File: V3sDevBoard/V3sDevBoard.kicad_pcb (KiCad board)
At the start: 2 copper layers, 100 x 80 mm, 197 parts, among them J1 JST_ETHERNET, J10 Power, J2 USB_C_Receptacle_USB2.0_16P, J3 USB_C_Receptacle_USB2.0_16P, J4 Micro_SD_Card_Det1, J5 LCD, J6 MIPI CSI, J7 JST_I2C, J8 AudioJack, J9 GPIO, SW1 BUT6, SW2 BUT1, SW3 BUT2, SW4 BUT3, SW5 BUT4, SW6 BUT5, U1 Allwinner_V3s, U10 MPU-6050, U11 BME280, U12 USBLC6-2SC6, U13 USBLC6-2SC6, U14 USBLC6-2SC6, U15 USBLC6-2SC6, U16 USBLC6-2SC6, U2 SY8089AAAC, U3 SY8089AAAC, U4 SY8089AAAC, U5 CH340C, U6 PT4103, U8 ESP32-WROOM-32, U9 Ai-Thinker-Ra-02, Y1 32768, Y2 24M

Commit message: first attempts to arrange components on a PCB
plus making footprints bme280&mpu6050 easier to hand solder.
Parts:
- BT1, C17: moved to B.Cu
- C43, C44: footprint Capacitor_SMD:C_0201_0603Metric_Pad0.64x0.40mm_HandSolder -> Capacitor_SMD:C_0603_1608Metric_Pad1.08x0.95mm_HandSolder
- L1, L2, L3, L4: footprint Inductor_SMD:L_APV_APH0420 -> Inductor_SMD:L_APV_APH0420_HandSolder
- Y1: value 32768 -> 24M; footprint Crystal:Crystal_SMD_Abracon_ABS25-4Pin_8.0x3.8mm -> Crystal:Crystal_SMD_3225-4Pin_3.2x2.5mm_HandSoldering
- Y2: footprint Crystal:Crystal_HC49-4H_Vertical -> Crystal:Crystal_SMD_3225-4Pin_3.2x2.5mm_HandSoldering
- moved D5 252.6 mm to (268.0, 109.5)
- moved D6 252.6 mm to (268.0, 116.1)
- moved D7 252.6 mm to (268.0, 122.7)
- moved D8 252.6 mm to (268.0, 129.4)
- moved SW1 242.4 mm to (219.4, 145.0), turned to -90 degrees
- moved TP14 215.9 mm to (260.2, 119.7)
- moved TP16 215.9 mm to (260.2, 122.7)
- moved TP17 215.9 mm to (260.2, 125.8)
- moved TP13 215.9 mm to (260.2, 116.6)
- moved TP9 215.9 mm to (260.2, 113.5)
- moved R36 215.3 mm to (237.2, 128.8)
- moved SW6 214.6 mm to (211.0, 145.0), turned to -90 degrees
- moved SW5 210.7 mm to (202.5, 145.0), turned to -90 degrees
- moved SW4 207.1 mm to (193.8, 145.0), turned to -90 degrees
- moved SW3 204.2 mm to (185.0, 145.0), turned to -90 degrees
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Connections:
- net LCD_LED_A renamed LED_A
- net LCD_LED_K renamed LED_K
- Y1 pad 1: Net-(U1B-X32KOUT) -> unconnected-(Y1-Pad1)
- Y1 pad 2: (no net) -> Net-(U1B-X32KIN)
- Y1 pad 3: (no net) -> unconnected-(Y1-Pad3)
- Y1 pad 4: Net-(U1B-X32KIN) -> Net-(U1B-X32KOUT)
- Y2 pad 1: Net-(U1B-X24MOUT) -> unconnected-(Y2-Pad1)
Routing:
- net GND: track 0.00 -> 69.4 mm, vias 0 -> 4
- net +3.3V: track 0.00 -> 52.7 mm, vias 0 -> 1
- net +1.8V: track 0.00 -> 31.3 mm
- net +1.2V: track 0.00 -> 31.3 mm
- net Net-(JP7-A): track 0.00 -> 28.6 mm
- net Net-(JP5-A): track 0.00 -> 27.8 mm
- net Net-(JP4-A): track 0.00 -> 27.8 mm
- net Net-(JP3-B): track 0.00 -> 13.8 mm
- net Net-(J7-Pin_1): track 0.00 -> 11.5 mm
- net Net-(U3-FB): track 0.00 -> 10.0 mm
- net Net-(U4-FB): track 0.00 -> 10.0 mm
- net Net-(U2-FB): track 0.00 -> 9.06 mm
- net Net-(U11-CSB): track 0.00 -> 7.82 mm
- net Net-(JP2-A): track 0.00 -> 6.34 mm
- net RA_RESET: track 0.00 -> 5.47 mm
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
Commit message: completing pcb desgin
Returning to project after month away. Switching to 4-layer desgin on 3313 stackup sig-gnd-pow-sig, changing size of some passive to 0603, connecting all components, adding silkscreen.
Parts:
- removed C10: 860u, Capacitor_THT:CP_Radial_D6.3mm_P2.50mm
- removed F1: PCB fuse, Fuse:Fuse_1206_3216Metric
- removed J10: Power, Connector_PinHeader_2.54mm:PinHeader_1x02_P2.54mm_Vertical
- removed R24, R25, R26, R27: 150R, Resistor_SMD:R_0805_2012Metric_Pad1.20x1.40mm_HandSolder
- removed TP18: CAM_IO0, TestPoint:TestPoint_Pad_D1.0mm
- removed TP3: ESPTX, TestPoint:TestPoint_Pad_D1.0mm
- removed TP4: EXPRX, TestPoint:TestPoint_Pad_D1.0mm
- added C22: 100n, Capacitor_SMD:C_0805_2012Metric_Pad1.18x1.45mm_HandSolder, F.Cu at (235.3, 123.8)
- added G***: LOGO, Lib:linux, F.Cu at (233.8, 134.2)
- BT1: footprint Battery:BatteryHolder_MYOUNG_BS-07-A1BJ001_CR2032 -> Connector_PinHeader_1.00mm:PinHeader_1x02_P1.00mm_Vertical_SMD_Pin1Right
- C27, C28, C30, C31, C33, C34, C35, C41, C42: footprint Capacitor_SMD:C_0805_2012Metric_Pad1.18x1.45mm_HandSolder -> Capacitor_SMD:C_0603_1608Metric_Pad1.08x0.95mm_HandSolder
- C32, C36, C37, C38, C39, D5, D6, D7, D8, J4, TP13, TP14, TP16, TP17, TP9: moved to B.Cu
- J9: value GPIO -> Conn_01x07_Pin; footprint Connector_PinHeader_2.54mm:PinHeader_1x10_P2.54mm_Vertical -> Connector_PinHeader_2.54mm:PinHeader_1x07_P2.54mm_Vertical
- R1, R10, R11, R12, R13, R2, R20, R21, R23, R28, R29, R3, R30, R31, R32, R33, R34, R35, R36, R37, R38, R39, R4, R40, R41, R42, R44, R45, R48, R49, R5, R50, R51, R52, R53, R54, R55, R56, R58, R6, R60, R61, R62, R68, R69, R70, R71, R72, R8, R9: footprint Resistor_SMD:R_0805_2012Metric_Pad1.20x1.40mm_HandSolder -> Resistor_SMD:R_0603_1608Metric_Pad0.98x0.95mm_HandSolder
- R14, R15, R16, R17, R18: footprint Resistor_SMD:R_0805_2012Metric_Pad1.20x1.40mm_HandSolder -> Resistor_SMD:R_0603_1608Metric_Pad0.98x0.95mm_HandSolder; moved to B.Cu
- R46, R47: footprint Resistor_SMD:R_1206_3216Metric -> Resistor_SMD:R_0805_2012Metric
- SW1, SW2, SW3, SW4, SW5, SW6: footprint Button_Switch_THT:SW_PUSH_6mm -> Button_Switch_SMD:Button_6x3mm
- U12, U13, U14, U15, U16: value USBLC6-2SC6 -> USBLC6
- Y1: value 24M -> 32K
- moved R35 209.6 mm to (240.0, 75.2)
- moved R28 207.5 mm to (230.3, 104.0), turned to -90 degrees
- moved R71 204.6 mm to (241.0, 101.3), turned to 90 degrees
- moved R72 202.1 mm to (239.0, 101.3), turned to -90 degrees
- moved R62 200.9 mm to (235.4, 104.0), turned to -90 degrees
- moved R61 199.7 mm to (232.8, 104.0), turned to -90 degrees
- moved R32 190.4 mm to (218.6, 86.9), turned to -90 degrees
- moved R30 188.6 mm to (213.8, 86.9), turned to -90 degrees
- moved R33 188.4 mm to (217.0, 86.9), turned to -90 degrees
- moved R31 186.8 mm to (212.2, 86.9), turned to -90 degrees
- moved R34 186.4 mm to (215.4, 86.9), turned to -90 degrees
- moved J9 184.7 mm to (227.8, 108.4), turned to 90 degrees
- moved C29 172.8 mm to (242.3, 77.5)
- moved JP1 170.2 mm to (238.0, 77.5)
- moved R68 164.7 mm to (186.0, 136.0), turned to 90 degrees
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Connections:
- C11 pad 1: EPHY-RX- -> Net-(C11-Pad1)
- C12 pad 1: EPHY-RX+ -> Net-(C12-Pad1)
- C13 pad 1: EPHY-TX- -> Net-(C13-Pad1)
- C14 pad 1: EPHY-TX+ -> Net-(C14-Pad1)
- D5 pad 1: VCC -> +3.3V
- D6 pad 1: VCC -> +3.3V
- D7 pad 1: VCC -> +3.3V
- D8 pad 1: VCC -> +3.3V
- J7 pad 2: TWI0_SDA -> Net-(J7-Pin_2)
- J7 pad 3: TWI0_SCK -> Net-(J7-Pin_3)
- J9 pad 1: Net-(J9-Pin_1) -> GND
- J9 pad 5: Net-(J9-Pin_5) -> VCC
- J9 pad 6: Net-(J9-Pin_6) -> +3.3V
- J9 pad 7: Net-(J9-Pin_7) -> GND
- R28 pad 2: Net-(J9-Pin_5) -> Net-(J9-Pin_2)
- R44 pad 2: VCC -> Net-(U12-VBUS)
- R45 pad 1: VCC -> Net-(U12-VBUS)
- R61 pad 2: Net-(J9-Pin_6) -> Net-(J9-Pin_3)
- R62 pad 2: Net-(J9-Pin_7) -> Net-(J9-Pin_4)
- U14 pad 4: EPHY-RX+ -> Net-(C12-Pad1)
- U14 pad 6: EPHY-RX- -> Net-(C11-Pad1)
- U15 pad 4: EPHY-TX+ -> Net-(C14-Pad1)
- U15 pad 6: EPHY-TX- -> Net-(C13-Pad1)
- U16 pad 4: TWI0_SCK -> Net-(J7-Pin_3)
- U16 pad 5: Net-(J7-Pin_1) -> +3.3V
- U16 pad 6: TWI0_SDA -> Net-(J7-Pin_2)
- Y1 pad 1: unconnected-(Y1-Pad1) -> GND
- Y1 pad 3: unconnected-(Y1-Pad3) -> GND
- Y2 pad 1: unconnected-(Y2-Pad1) -> GND
- Y2 pad 3: unconnected-(Y2-Pad3) -> GND
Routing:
- net VCC: track 0.00 -> 157.6 mm, vias 0 -> 2
- net GND: track 69.4 -> 222.3 mm, vias 4 -> 126
- net TWI0_SDA: track 3.34 -> 142.3 mm, vias 0 -> 6
- net TWI0_SCK: track 3.30 -> 131.3 mm, vias 0 -> 4
- net LED_A: track 0.00 -> 99.6 mm, vias 0 -> 1
- net +3.3V: track 52.7 -> 150.5 mm, vias 1 -> 40
- net +1.2V: track 31.3 -> 127.1 mm, vias 0 -> 14
- net LED_K: track 0.00 -> 89.9 mm, vias 0 -> 1
- net HPCOM: track 0.00 -> 77.3 mm, vias 0 -> 2
- net LCD_LED_PWM: track 0.00 -> 75.3 mm, vias 0 -> 2
- net +1.8V: track 31.3 -> 105.8 mm, vias 0 -> 9
- net UART0_TX: track 0.00 -> 73.8 mm, vias 0 -> 2
- net CSI_SCK: track 0.00 -> 73.5 mm, vias 0 -> 3
- net Net-(D6-DOUT): track 0.00 -> 73.0 mm
- net CSI_SDA: track 0.00 -> 72.7 mm, vias 0 -> 3
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- added copper zone on In2.Cu, net +3.3V
- added copper zone on In1.Cu, net GND
- added copper zone on In2.Cu, net GND
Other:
- board size 100 x 80 mm -> 100 x 85 mm
- copper layers 2 -> 4
- board text added: "GND 3V3 VCC SDA SCK PF6 GND"
- board text added: "GND PF6 SCK SDA VCC 3V3 GND"
- board text added: "J.K 2026.02 V3sDevBoard rev.A"
- board text added: "V3sDevBoard"
- board text added: "github.com/sentoxo/V3sDevBoard"

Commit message: last changes and sending to manufacturing
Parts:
- added R24: 1K, Resistor_SMD:R_0603_1608Metric_Pad0.98x0.95mm_HandSolder, F.Cu at (220.1, 86.9)
- moved D1 1.66 mm to (215.3, 80.9)
- moved C24 1.33 mm to (216.2, 96.1)
- moved C25 1.33 mm to (216.2, 98.3)
- moved R29 1.33 mm to (216.1, 94.3)
- moved R64 0.53 mm to (184.4, 96.4)
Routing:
- net +3.3V: track 150.5 -> 148.0 mm
- net LCD_VSYNC: track 11.1 -> 9.79 mm
- net +3V: track 42.3 -> 41.0 mm
- net GND: track 222.3 -> 221.1 mm, vias 126 -> 128
- net ESP32_UART_RX: track 55.4 -> 54.4 mm
- net Net-(U1A-VRA2): track 14.9 -> 14.1 mm
- net SDC1_D2: track 35.7 -> 36.5 mm
- net Net-(U1A-VRA1): track 12.3 -> 11.6 mm
- net LCD_HSYNC: track 13.8 -> 13.1 mm
- net ESP32_UART_TX: track 58.4 -> 57.7 mm
- net LCD_CLK: track 8.12 -> 7.42 mm
- net LCD_B7: track 18.9 -> 19.5 mm

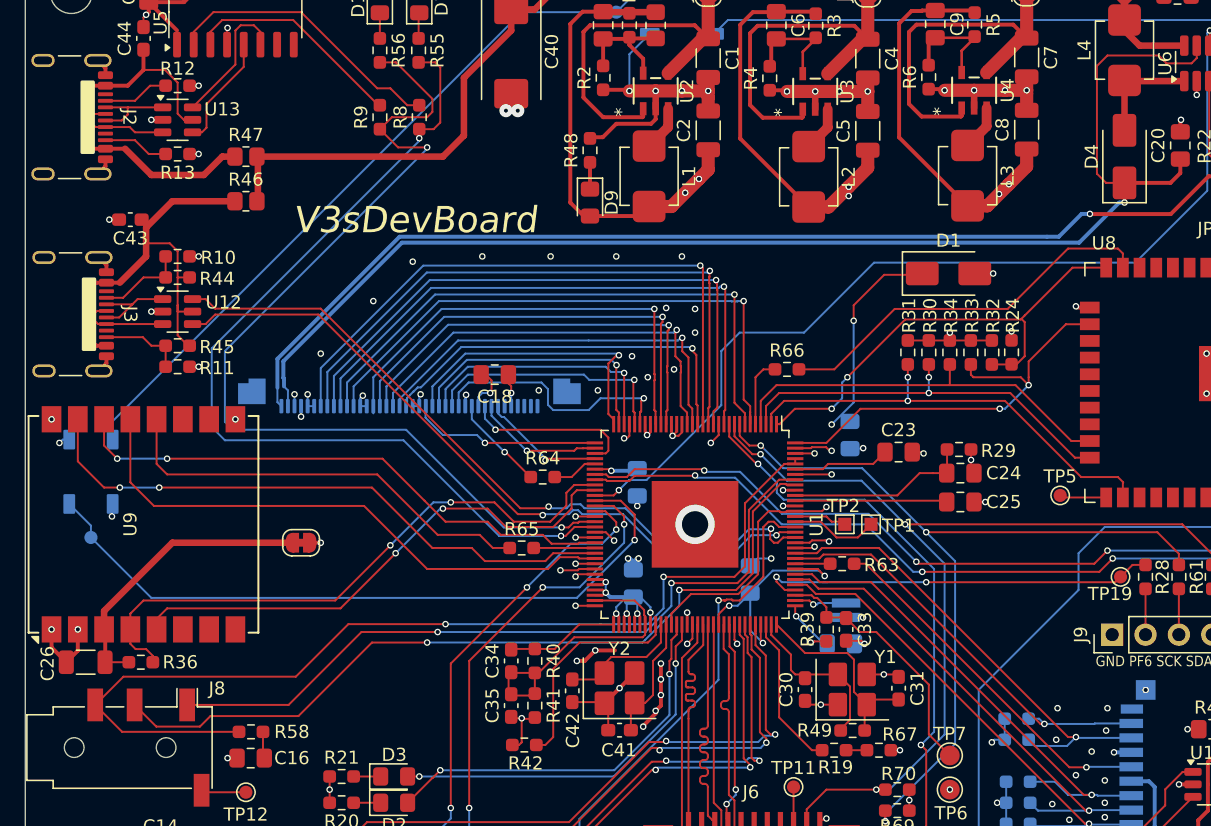
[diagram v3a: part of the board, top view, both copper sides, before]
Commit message: fixing errors in revA
Fixing:
- Ther was mistake in SDIO for SDCard. Swaped data lines.
- RTC didn't have power without battery.
Updating readme.
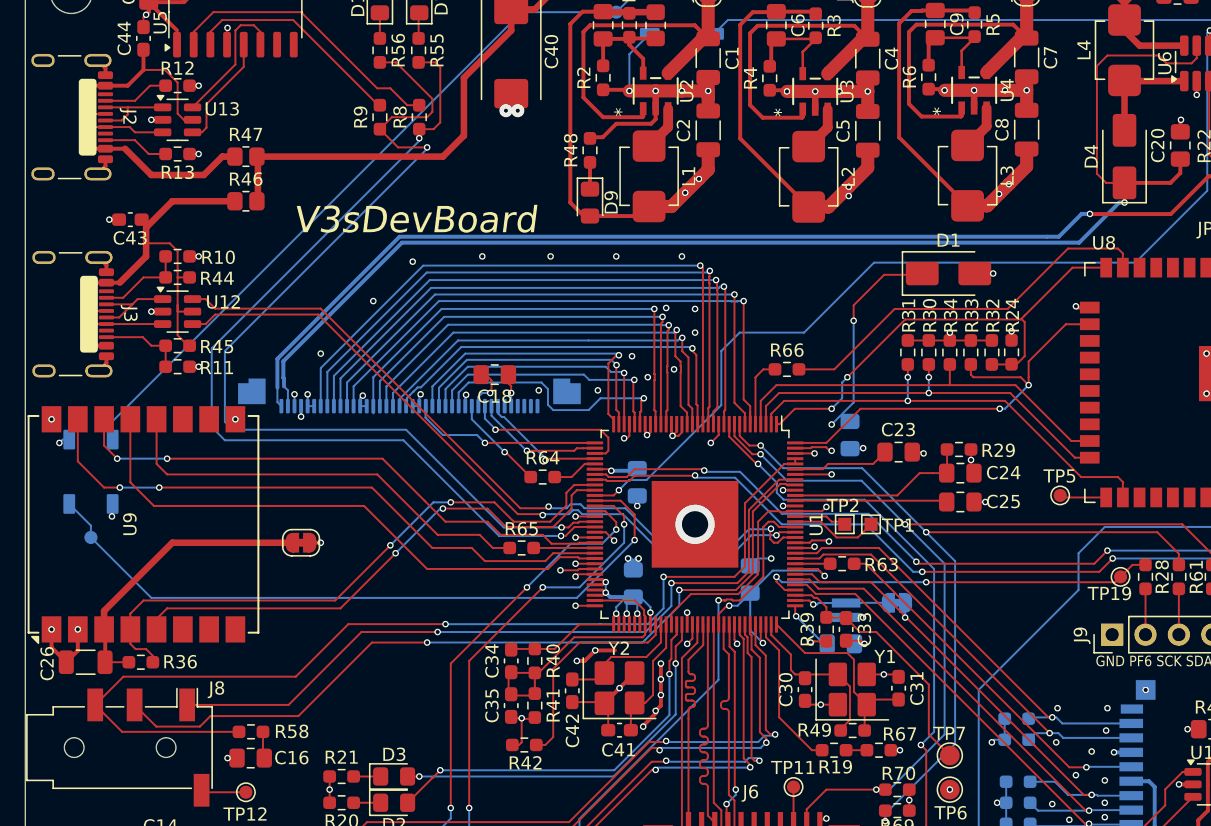
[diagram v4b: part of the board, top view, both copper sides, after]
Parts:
- added JP6: vcc-rtc, Jumper:SolderJumper-2_P1.3mm_Bridged_RoundedPad1.0x1.5mm, B.Cu at (211.4, 106.0)
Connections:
- J4 pad 7: SDC0_D1 -> SDC0_D0
- J4 pad 8: SDC0_D0 -> SDC0_D1
- R14 pad 2: SDC0_D0 -> SDC0_D1
- R15 pad 2: SDC0_D1 -> SDC0_D0
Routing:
- net Net-(BT1-+): track 4.05 -> 7.28 mm
- net SDC0_D1: track 35.8 -> 33.1 mm
- net SDC0_D0: track 32.4 -> 34.0 mm
- net +3.3V: track 148.0 -> 149.1 mm, vias 40 -> 41
